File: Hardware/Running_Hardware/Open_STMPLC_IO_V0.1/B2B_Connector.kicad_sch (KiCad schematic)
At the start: 29 parts, among them J1 Screw_Terminal_01x10, J2 Screw_Terminal_01x06, J39 10144517-041802LF, J41 10144517-041802LF, J42 10144517-041802LF, J43 Screw_Terminal_01x02, J9 DE9_Pins, Q5 AOD407, Q6 AOD407, Q7 MMBT5401

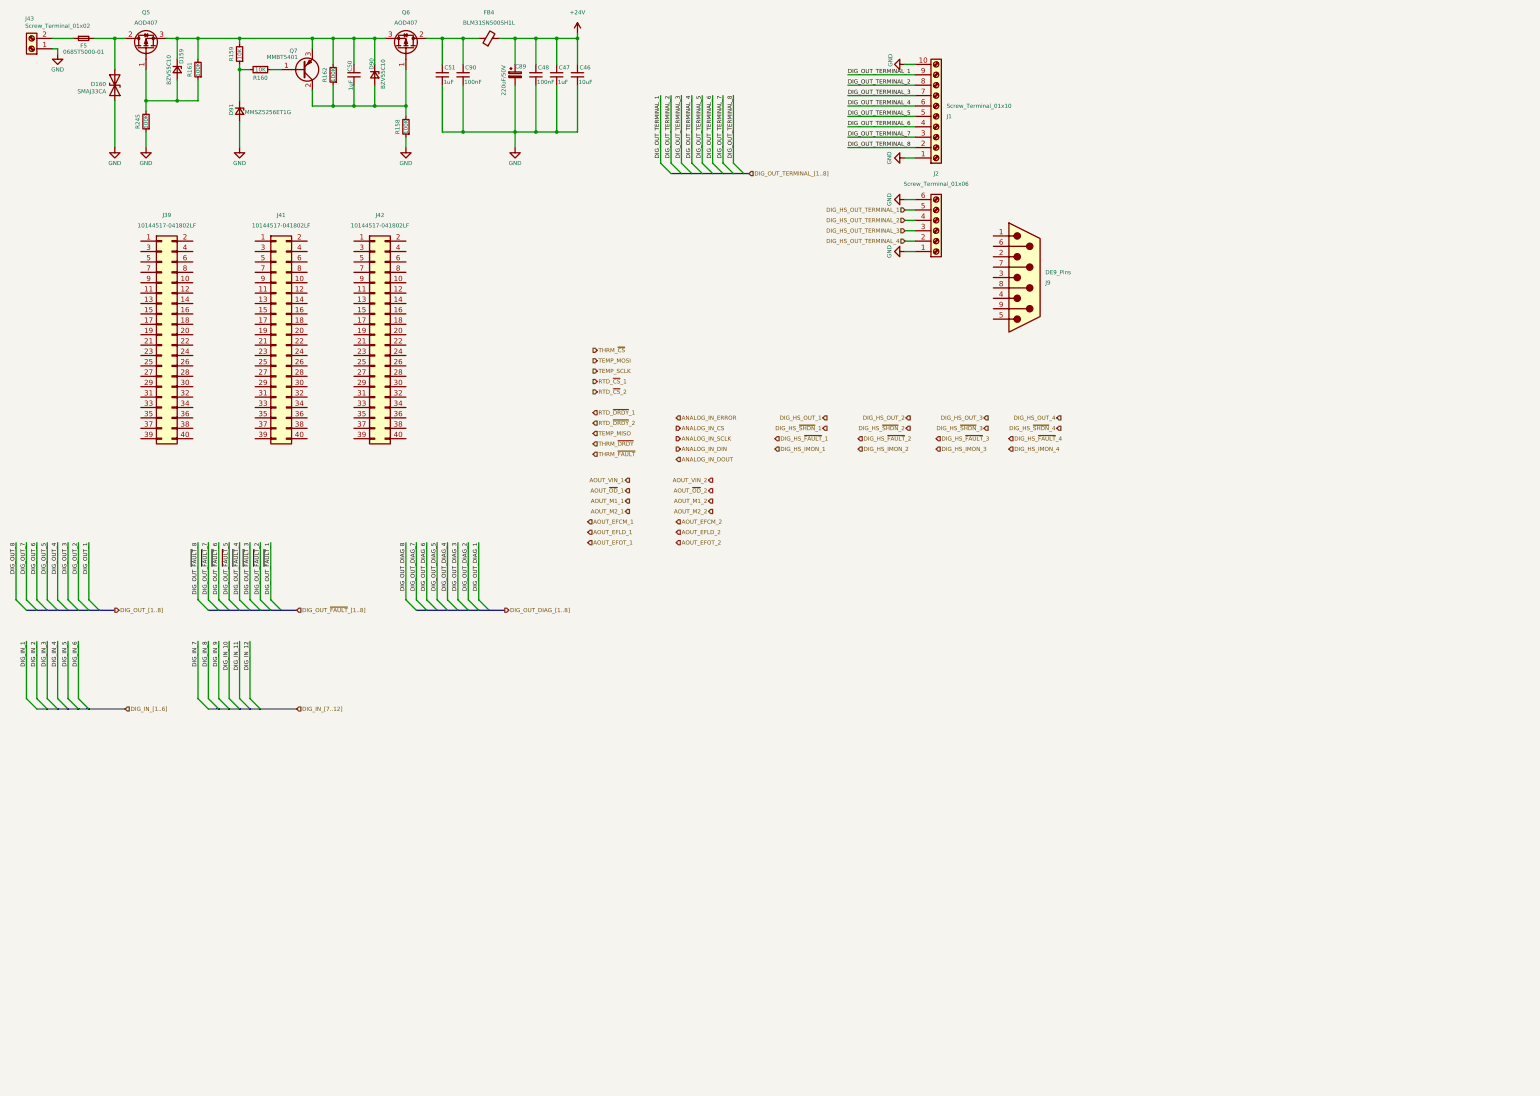
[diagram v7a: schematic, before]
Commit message: Pin mapping IO connector
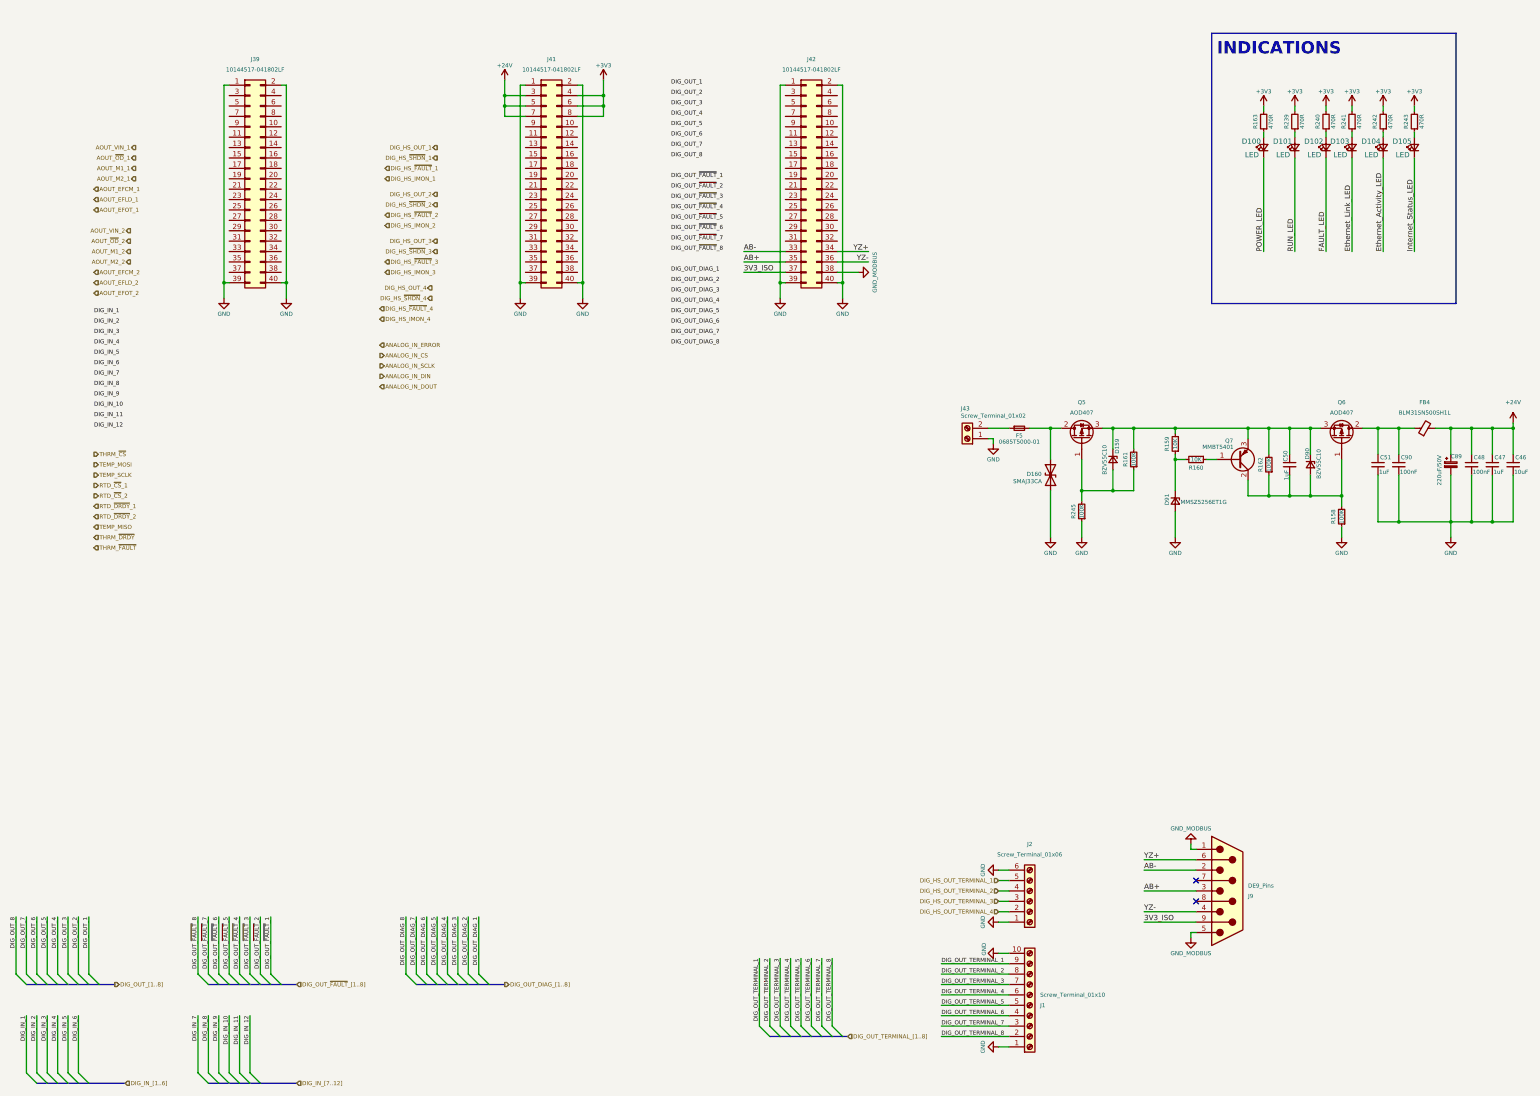
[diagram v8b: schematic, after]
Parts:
- added D100, D101, D102, D103, D104, D105: LED, LED_SMD:LED_0603_1608Metric_Pad1.05x0.95mm_HandSolder, symbol Device:LED_Small
- added R163, R239, R240, R241, R242, R243: 470R, Resistor_SMD:R_0603_1608Metric_Pad0.98x0.95mm_HandSolder, symbol Device:R_Small
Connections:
- net +24V: now also J41.3 (Pin_3), J41.5 (Pin_5), J41.7 (Pin_7)
- net GND: now also J39.1 (Pin_1), J39.2 (Pin_2), J39.39 (Pin_39), J39.40 (Pin_40), J41.1 (Pin_1), J41.2 (Pin_2), J41.39 (Pin_39), J41.40 (Pin_40), J42.1 (Pin_1), J42.2 (Pin_2), J42.39 (Pin_39), J42.40 (Pin_40)
- net AB-: now reaches J42.33 (Pin_33)
- net AB-: now also J9.2
- net YZ+: now reaches J42.34 (Pin_34)
- net YZ+: now also J9.6
- net AB+: now reaches J42.35 (Pin_35)
- net AB+: now also J9.3
- net YZ-: now reaches J42.36 (Pin_36)
- net YZ-: now also J9.4
- net 3V3_ISO: now reaches J42.37 (Pin_37)
- net 3V3_ISO: now also J9.9
- net GND_MODBUS: now reaches J42.38 (Pin_38)
- net GND_MODBUS: now also J9.1, J9.5
- net +3V3: now reaches J41.4 (Pin_4)
- net +3V3: now also J41.6 (Pin_6), J41.8 (Pin_8), R163.2, R239.2, R240.2, R241.2, R242.2, R243.2
- new net: D100.2 (A), R163.1
- new net: D104.2 (A), R242.1
- new net: D105.2 (A), R243.1
- new net: D103.2 (A), R241.1
- new net: D101.2 (A), R239.1
- new net: D102.2 (A), R240.1
- new net Ethernet_Activity_LED: D104.1 (K)
- new net Ethernet_Link_LED: D103.1 (K)
- new net FAULT_LED: D102.1 (K)
- new net Internet_Status_LED: D105.1 (K)
- new net POWER_LED: D100.1 (K)
- new net RUN_LED: D101.1 (K)
- no-connect marks 0 -> 2
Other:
- note added: "INDICATIONS"
- moved on the sheet: C46, C47, C48, C50, C51, C89, C90, D159, D160, D90, D91, F5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
